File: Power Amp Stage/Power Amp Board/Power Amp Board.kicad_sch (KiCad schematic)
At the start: 30 parts, among them J2 Conn_01x02, J3 Conn_01x02, Q1 BC549, Q2 BC559, Q3 MJ15004, Q4 MJ15003, Q5 MJ15004, Q6 MJ15003, U1 ADA4522-2ARMZ-R7

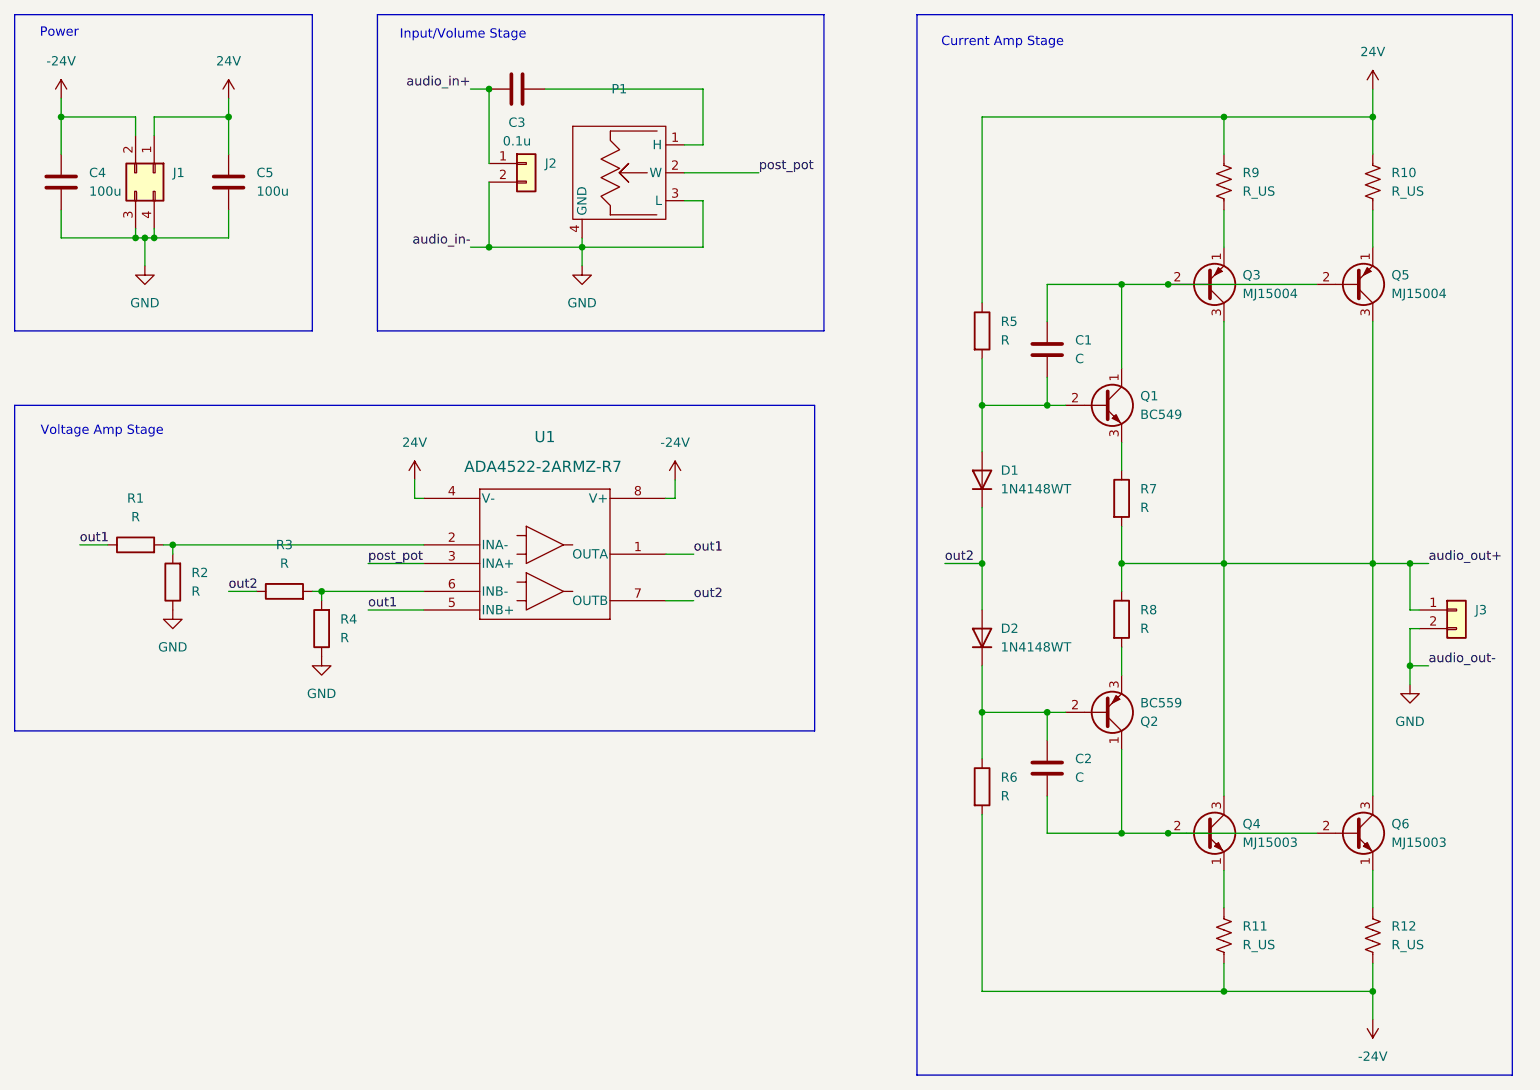
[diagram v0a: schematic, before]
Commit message: added buffer to schematic of power amp
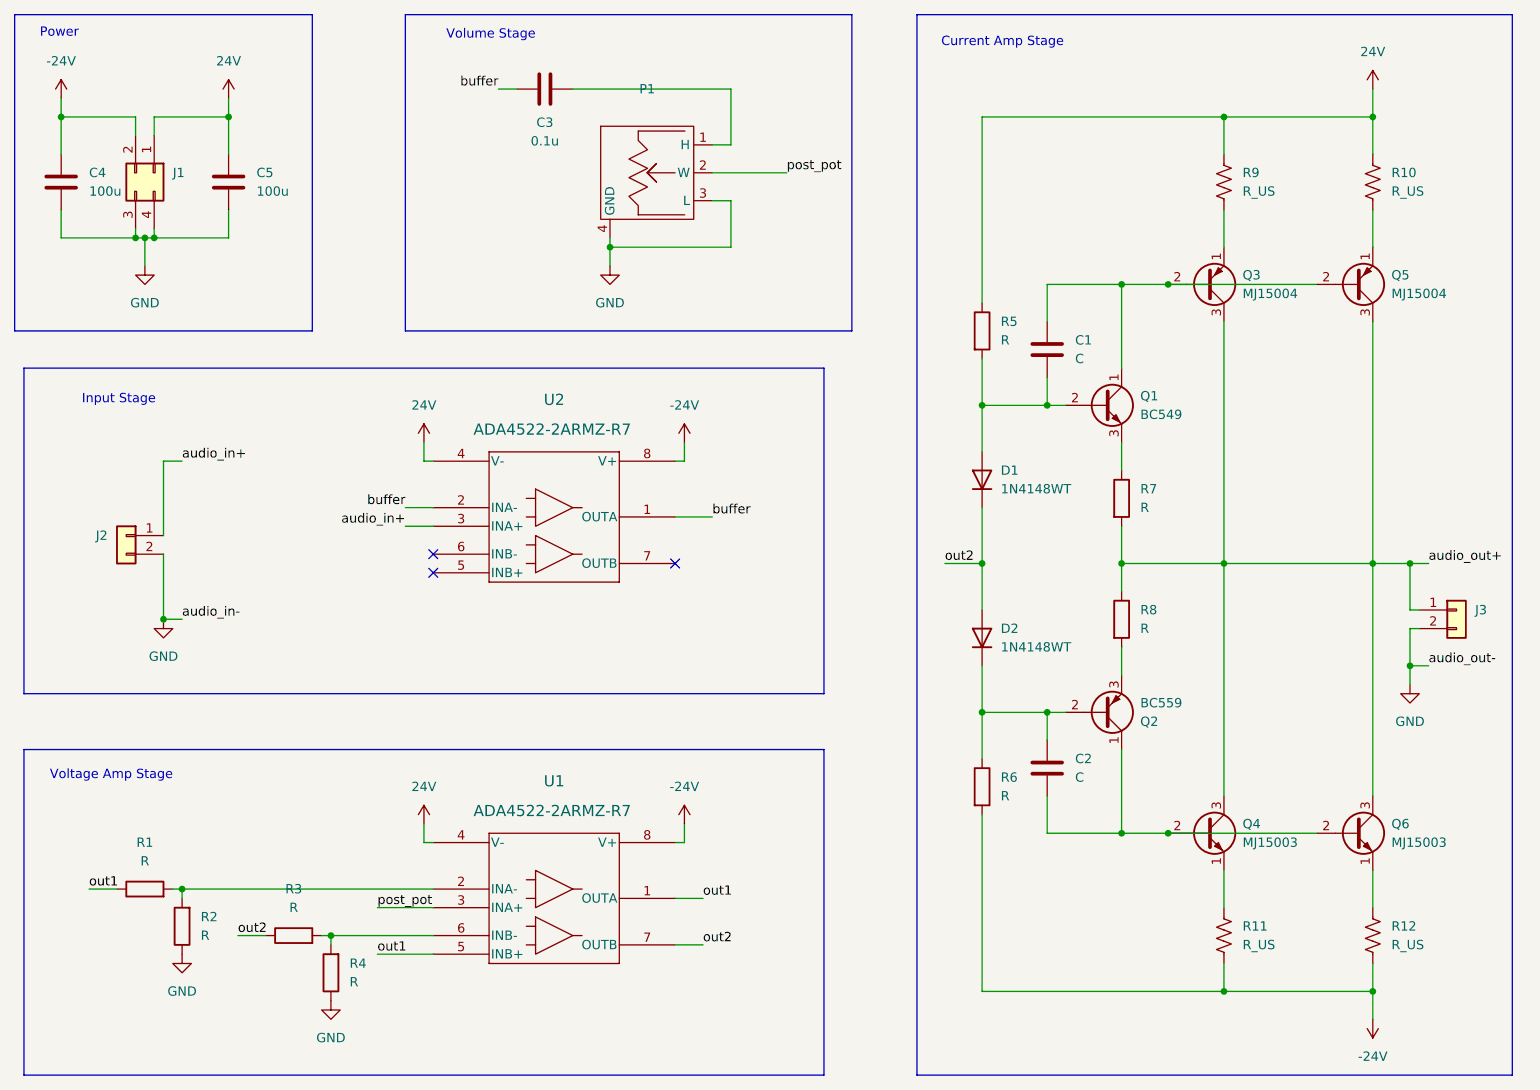
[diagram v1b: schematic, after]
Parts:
- added U2: ADA4522-2ARMZ-R7, GTSR_KiCAD_Footprints:RM-8_ADI, symbol Components:ADA4522-2ARMZ-R7
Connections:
- net -24V: now also U2.8 (V+)
- net 24V: now also U2.4 (V-)
- net audio_in+: now also U2.3 (INA+); no longer C3.1
- new net buffer: C3.1, U2.1 (OUTA), U2.2 (INA-)
- no-connect marks 0 -> 3
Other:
- note added: "Input Stage"
- note added: "Volume Stage"
- note removed: "Input/Volume Stage"
- moved on the sheet: C3, J2, P1, R1, R2, R3, R4, U1

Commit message: just absolutely lapped kyle
get fucked kyle
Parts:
- R1, R3: value R -> 100k
- R10, R11, R12, R9: value R_US -> 4.7
- R2, R4, R5, R6: value R -> 10k
- R7, R8: value R -> 100
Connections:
- net audio_in+: now also C3.1; no longer U2.3 (INA+)
- net buffer: now also P1.1 (H); no longer C3.1
- net at C3.2: now also U2.3 (INA+); no longer P1.1 (H)
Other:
- moved on the sheet: C3
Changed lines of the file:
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@@
 	(wire
 		(pts
-			(xy 90.17 38.1) (xy 92.71 38.1)
+			(xy 90.17 38.1) (xy 121.92 38.1)
 		)
 		(stroke
@@
 	(bus
 		(pts
-			(xy 25.4 120.65) (xy 134.62 120.65)
+			(xy 25.4 118.11) (xy 137.16 118.11)
 		)
 		(stroke
@@
 	(bus
 		(pts
-			(xy 25.4 76.2) (xy 25.4 120.65)
+			(xy 25.4 77.47) (xy 25.4 118.11)
 		)
 		(stroke
@@
 	(wire
 		(pts
+			(xy 64.77 97.79) (xy 69.85 97.79)
+		)
+		(stroke
+			(width 0)
+			(type default)
+		)
+	)
+	(wire
+		(pts
 			(xy 53.34 39.37) (xy 53.34 41.91)
 		)
@@
 	(wire
 		(pts
-			(xy 100.33 38.1) (xy 121.92 38.1)
-		)
-		(stroke
-			(width 0)
-			(type default)
-		)
-	)
-	(wire
-		(pts
 			(xy 114.3 148.59) (xy 118.11 148.59)
 		)
@@
 	(bus
 		(pts
-			(xy 134.62 120.65) (xy 134.62 76.2)
+			(xy 137.16 118.11) (xy 137.16 77.47)
 		)
 		(stroke
@@
 	(bus
 		(pts
-			(xy 25.4 76.2) (xy 134.62 76.2)
+			(xy 25.4 77.47) (xy 137.16 77.47)
 		)
 		(stroke
@@
 	(wire
 		(pts
-			(xy 77.47 97.79) (xy 81.28 97.79)
-		)
-		(stroke
-			(width 0)
-			(type default)
-		)
-	)
-	(wire
-		(pts
 			(xy 215.9 109.22) (xy 214.63 109.22)
 		)
@@
 	(wire
 		(pts
+			(xy 77.47 97.79) (xy 81.28 97.79)
+		)
+		(stroke
+			(width 0)
+			(type default)
+		)
+	)
+	(wire
+		(pts
 			(xy 189.23 41.91) (xy 189.23 46.99)
 		)
@@
 	)
 	(label "audio_in+"
-		(at 77.47 97.79 180)
+		(at 64.77 97.79 180)
 		(effects
 			(font
@@
 			)
 		)
-		(property "Value" "R"
+		(property "Value" "10k"
 			(at 158.75 134.6199 0)
 			(effects
@@
 			)
 		)
-		(property "Value" "R_US"
+		(property "Value" "4.7"
 			(at 191.77 52.0699 0)
 			(effects
@@
 			)
 		)
-		(property "Value" "R"
+		(property "Value" "10k"
 			(at 69.85 160.0199 0)
 			(effects
@@
 			)
 		)
-		(property "Value" "R"
+		(property "Value" "10k"
 			(at 49.53 153.6699 0)
 			(effects
@@
 			)
 		)
-		(property "Value" "R"
+		(property "Value" "100k"
 			(at 41.91 143.51 90)
 			(effects
@@
 			)
 		)
-		(property "Value" "R_US"
+		(property "Value" "4.7"
 			(at 212.09 154.9399 0)
 			(effects
@@
 			)
 		)
-		(property "Value" "R_US"
+		(property "Value" "4.7"
 			(at 212.09 52.0699 0)
 			(effects
@@
 			)
 		)
-		(property "Value" "R"
+		(property "Value" "100k"
 			(at 62.23 149.86 90)
 			(effects
@@
 			)
 		)
-		(property "Value" "R_US"
+		(property "Value" "4.7"
 			(at 191.77 154.9399 0)
 			(effects
@@
 			)
 		)
-		(property "Value" "R"
+		(property "Value" "100"
 			(at 177.8 111.7599 0)
 			(effects
@@
 	(symbol
 		(lib_id "Device:C")
-		(at 96.52 38.1 90)
+		(at 73.66 97.79 90)
 		(unit 1)
 		(exclude_from_sim no)
@@
 		(dnp no)
 		(property "Reference" "C3"
-			(at 96.52 42.672 90)
+			(at 73.66 102.362 90)
 			(effects
 				(font
@@
 		)
 		(property "Value" "0.1u"
-			(at 96.52 45.212 90)
+			(at 73.66 104.902 90)
 			(effects
 				(font
@@
 		)
 		(property "Footprint" "Capacitor_SMD:C_0603_1608Metric"
-			(at 100.33 37.1348 0)
+			(at 77.47 96.8248 0)
 			(effects
 				(font
@@
 		)
 		(property "Datasheet" "~"
-			(at 96.52 38.1 0)
+			(at 73.66 97.79 0)
 			(effects
 				(font
@@
 		)
 		(property "Description" "Unpolarized capacitor"
-			(at 96.52 38.1 0)
+			(at 73.66 97.79 0)
 			(effects
 				(font
@@
 		)
 		(instances
-			(project ""
+			(project "Power Amp Board"
 				(path "/3635e7f8-232c-4664-ad49-5c0692c6759f"
 					(reference "C3")
@@
 			)
 		)
-		(property "Value" "R"
+		(property "Value" "100"
 			(at 177.8 95.2499 0)
 			(effects
@@
 			)
 		)
-		(property "Value" "R"
+		(property "Value" "10k"
 			(at 158.75 72.3899 0)
 			(effects

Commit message: fixed board again
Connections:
- net -24V: now also J1.4 (Pin_4); no longer J1.2 (Pin_2)
- net 24V: now also J1.3 (Pin_3); no longer J1.1 (Pin_1)
- net GND: now also J1.1 (Pin_1), J1.2 (Pin_2), J2.1 (Pin_1), J3.1 (Pin_1); no longer J1.3 (Pin_3), J1.4 (Pin_4), J2.2 (Pin_2), J3.2 (Pin_2)
- net audio_in+: now also J2.2 (Pin_2); no longer J2.1 (Pin_1)
- net audio_out+: now also J3.2 (Pin_2); no longer J3.1 (Pin_1)
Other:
- moved on the sheet: J1, J2

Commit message: Update Power Amp Board.kicad_sch
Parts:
- C1, C2: value C -> 0.001u
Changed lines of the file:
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@@
 			)
 		)
-		(property "Value" "C"
+		(property "Value" "0.001u"
 			(at 168.91 132.0799 0)
 			(effects
@@
 			)
 		)
-		(property "Value" "C"
+		(property "Value" "0.001u"
 			(at 168.91 74.9299 0)
 			(effects
